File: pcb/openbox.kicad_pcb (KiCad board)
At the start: 2 copper layers, 24 parts

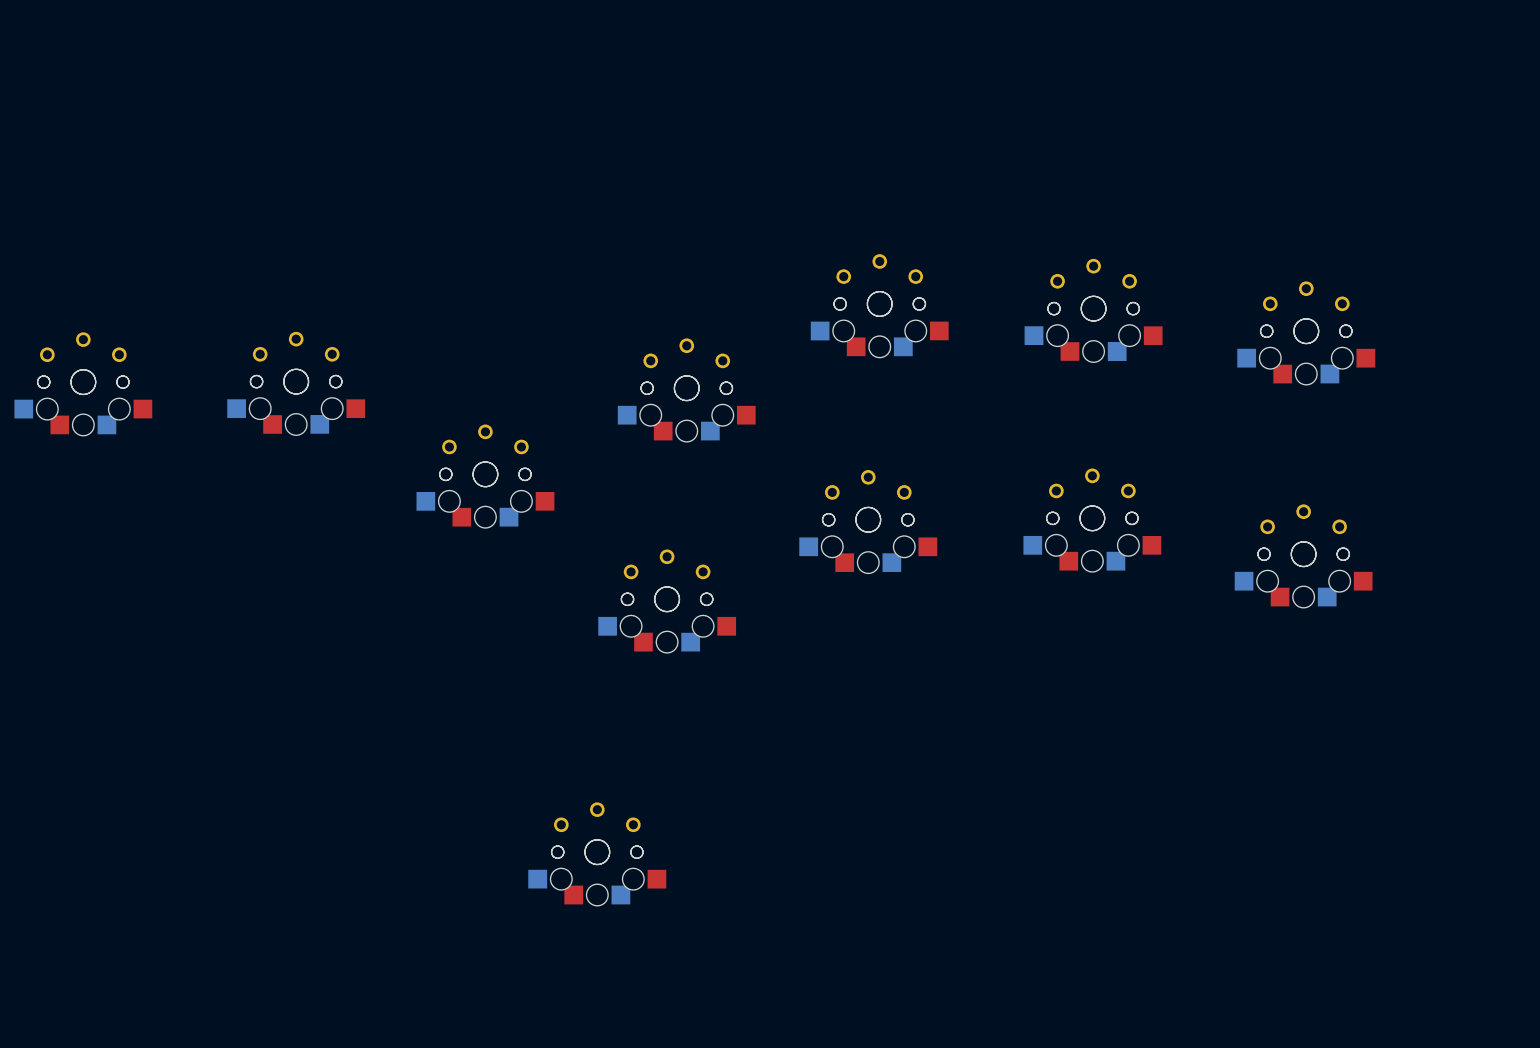
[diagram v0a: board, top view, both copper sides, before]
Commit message: Pi placed, just have to place buttons
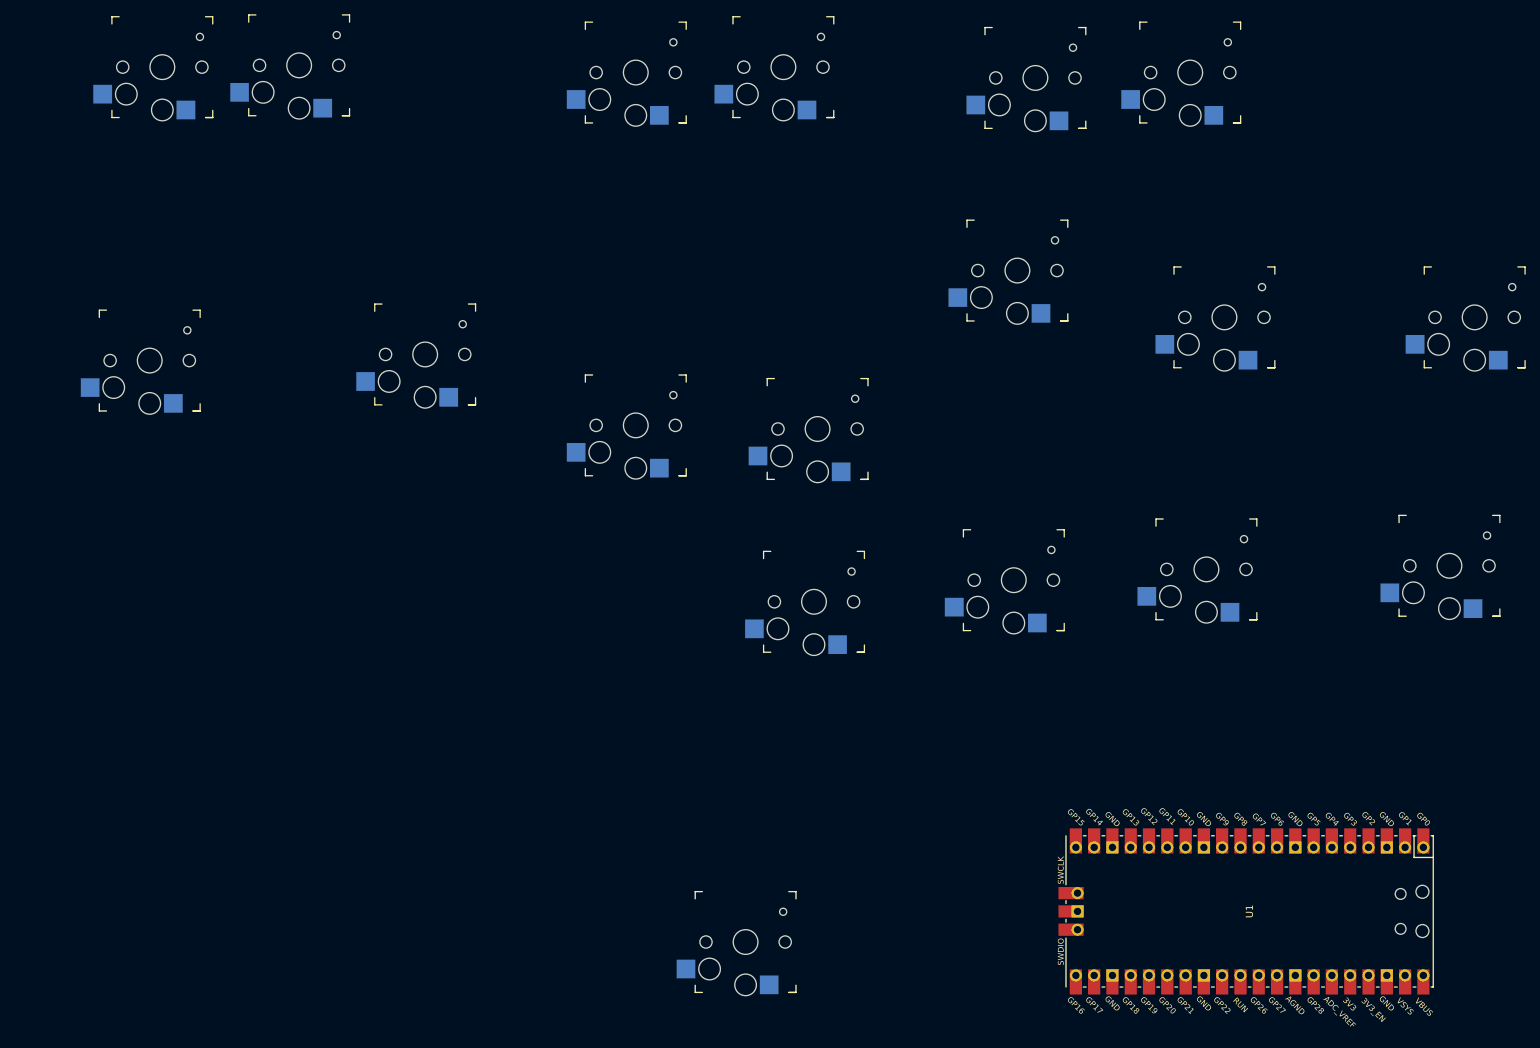
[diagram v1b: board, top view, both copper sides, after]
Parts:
- removed S33 (x12), S34 (x12): , PG1350
- added CAPTURE1: SW_SPST, keyswitches.pretty:Kailh_socket_PG1350, F.Cu at (142.8, 26.5)
- added DOWN1: SW_SPST, keyswitches.pretty:Kailh_socket_PG1350, F.Cu at (93.0, 66.4)
- added HOME1: SW_SPST, keyswitches.pretty:Kailh_socket_PG1350, F.Cu at (122.2, 27.2)
- added K1: SW_SPST, keyswitches.pretty:Kailh_socket_PG1350, F.Cu at (147.0, 100.8)
- added K2: SW_SPST, keyswitches.pretty:Kailh_socket_PG1350, F.Cu at (174.8, 97.8)
- added K3: SW_SPST, keyswitches.pretty:Kailh_socket_PG1350, F.Cu at (201.5, 96.2)
- added K4: SW_SPST, keyswitches.pretty:Kailh_socket_PG1350, F.Cu at (235.2, 95.8)
- added L3: SW_SPST, keyswitches.pretty:Kailh_socket_PG1350, F.Cu at (177.8, 28.0)
- added LEFT1: SW_SPST, keyswitches.pretty:Kailh_socket_PG1350, F.Cu at (54.8, 67.2)
- added P1: SW_SPST, keyswitches.pretty:Kailh_socket_PG1350, F.Cu at (147.5, 76.8)
- added P2: SW_SPST, keyswitches.pretty:Kailh_socket_PG1350, F.Cu at (175.2, 54.8)
- added P3: SW_SPST, keyswitches.pretty:Kailh_socket_PG1350, F.Cu at (204.0, 61.2)
- added P4: SW_SPST, keyswitches.pretty:Kailh_socket_PG1350, F.Cu at (238.8, 61.2)
- added R3: SW_SPST, keyswitches.pretty:Kailh_socket_PG1350, F.Cu at (199.2, 27.2)
- added RIGHT1: SW_SPST, keyswitches.pretty:Kailh_socket_PG1350, F.Cu at (122.2, 76.2)
- added SELECT1: SW_SPST, keyswitches.pretty:Kailh_socket_PG1350, F.Cu at (75.5, 26.2)
- added START1: SW_SPST, keyswitches.pretty:Kailh_socket_PG1350, F.Cu at (56.5, 26.5)
- added U1: Pico, MCU_RaspberryPi_and_Boards:RPi_Pico_SMD_TH, F.Cu at (207.5, 143.8)
- added UP1: SW_SPST, keyswitches.pretty:Kailh_socket_PG1350, F.Cu at (137.5, 148.0)

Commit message: Change extra buttons to 6x6mm push buttons
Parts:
- CAPTURE1, HOME1, L3, R3, SELECT1, START1: footprint keyswitches.pretty:Kailh_socket_PG1350 -> Button_Switch_THT:SW_PUSH_6mm
- moved LEFT1 9.25 mm to (62.0, 73.0)
